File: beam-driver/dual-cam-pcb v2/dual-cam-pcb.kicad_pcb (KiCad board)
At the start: 2 copper layers, 76 x 51 mm, 45 parts, among them J1 Conn_01x08_Pin, J2 Conn_01x08_Pin, J3 Conn_Coaxial, J4 LED connector, J5 LED connector, J6 tilt, J7 pan, J8 Conn_XT_Sink, Q1 Q_NMOS_GDS, U1 Pico, U2 PUCC27624DR, U3 LM317L_SOT-89, U4 LM7805_TO220

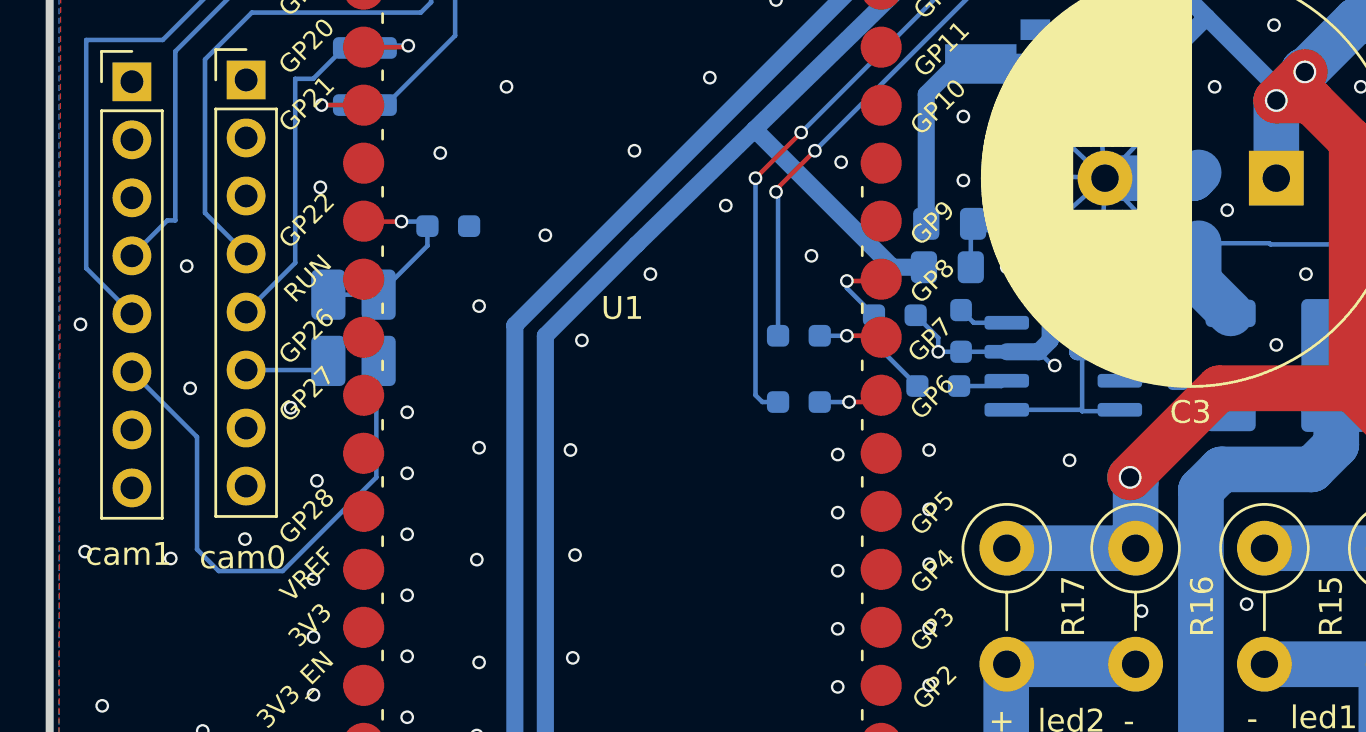
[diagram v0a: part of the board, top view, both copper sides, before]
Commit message: update beam-driver pcb
to include emi filter on ExposureActive camera GPIO.
+ update gerbers
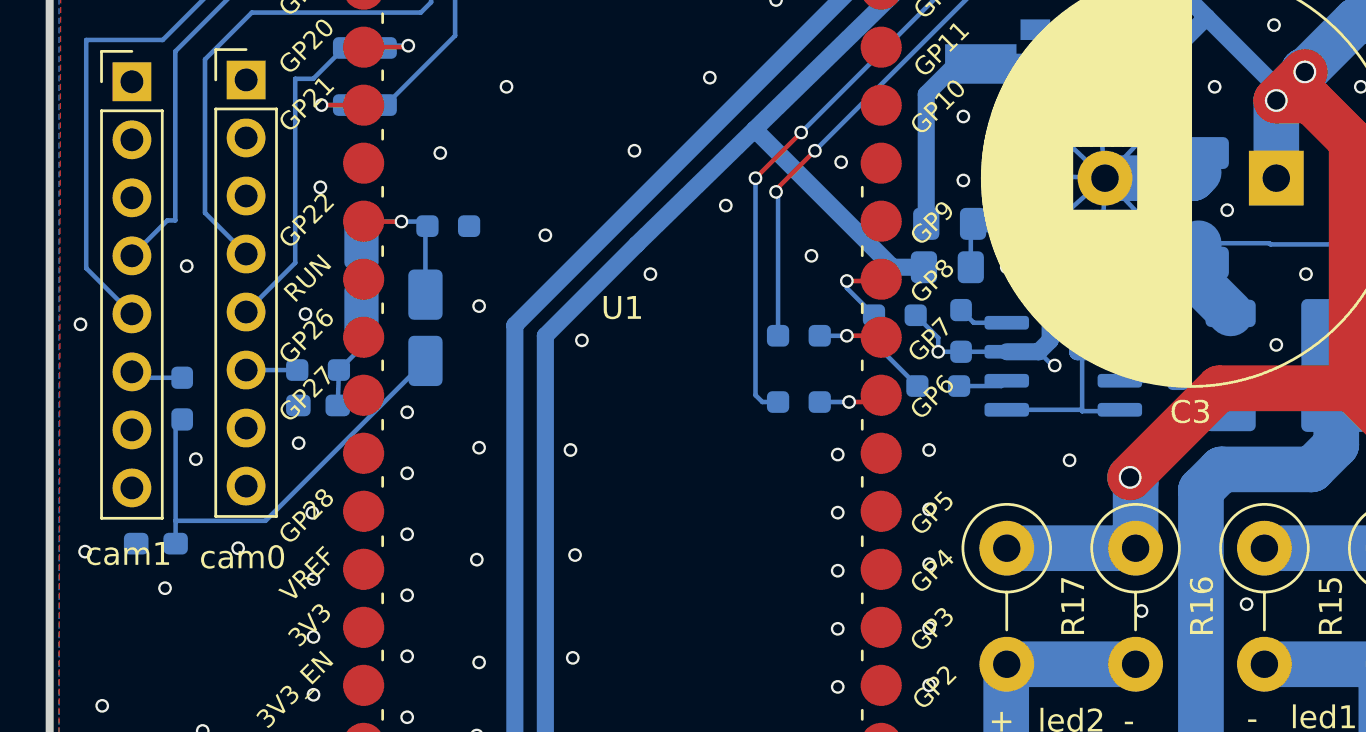
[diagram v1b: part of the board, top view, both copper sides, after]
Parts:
- added C8: 200pF, Capacitor_SMD:C_0603_1608Metric_Pad1.08x0.95mm_HandSolder, B.Cu at (78.5, 92.0)
- added C9: 200pF, Capacitor_SMD:C_0603_1608Metric_Pad1.08x0.95mm_HandSolder, B.Cu at (85.7, 86.0)
- added R20: 1k, Resistor_SMD:R_0603_1608Metric_Pad0.98x0.95mm_HandSolder, B.Cu at (79.7, 85.7)
- added R21: 1k, Resistor_SMD:R_0603_1608Metric_Pad0.98x0.95mm_HandSolder, B.Cu at (85.7, 84.4)
- R1: value 10k -> 20k
- R10: value 10k -> 510
- R12: footprint Resistor_SMD:R_1206_3216Metric_Pad1.30x1.75mm_HandSolder -> Resistor_SMD:R_2010_5025Metric_Pad1.40x2.65mm_HandSolder
- R9: value 10k -> 4k3
- moved D1 2.68 mm to (87.5, 80.3)
- moved D2 2.05 mm to (90.3, 82.5)
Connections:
- J1 pad 6: Net-(D1-A) -> Net-(J1-Pin_6)
- J2 pad 6: Net-(D2-A) -> Net-(J2-Pin_6)
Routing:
- net Net-(D2-A): track 24.0 -> 19.4 mm
- net Net-(J2-Pin_6): track 0.00 -> 2.31 mm
- net Net-(J1-Pin_6): track 0.00 -> 2.24 mm
- net Net-(D1-K): track 9.07 -> 8.16 mm
- net Net-(D1-A): track 3.77 -> 4.61 mm
- net GND: vias 126 -> 127

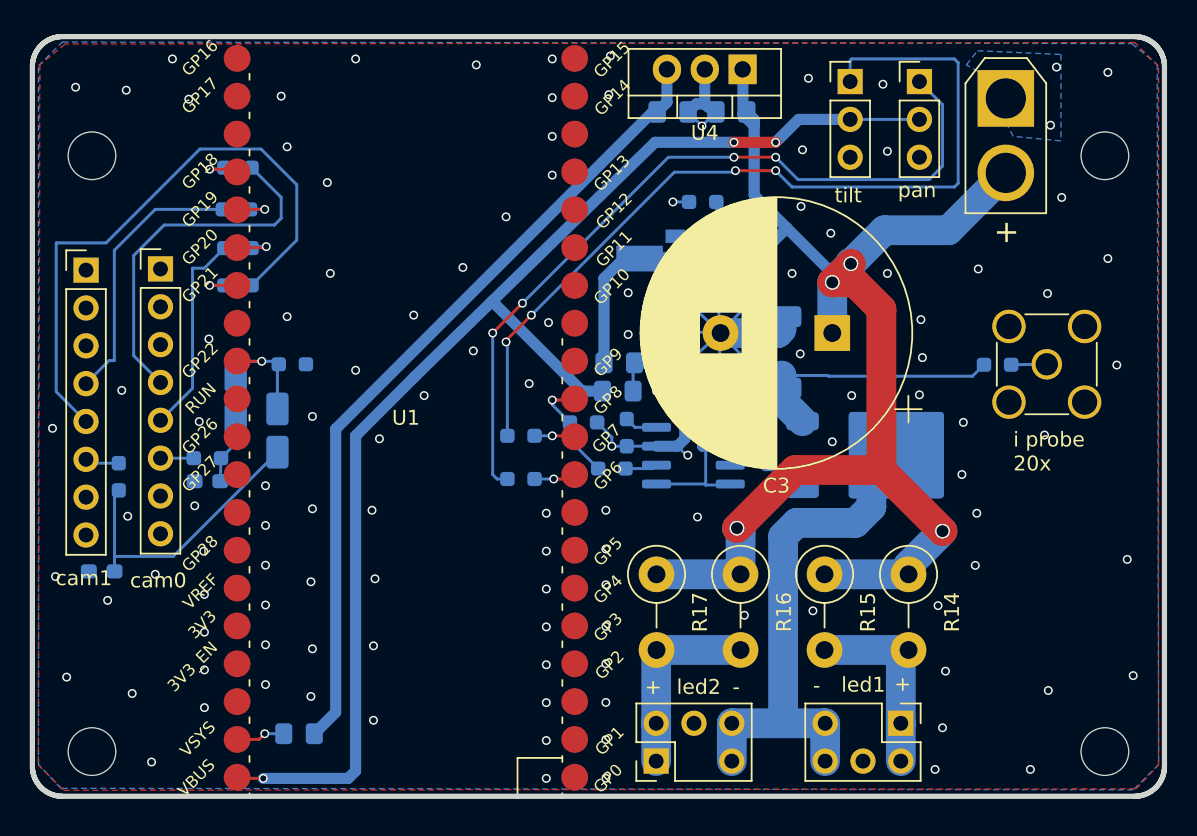
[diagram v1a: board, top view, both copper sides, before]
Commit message: update dual-cam-pcb
* change some footprints
* add miller capacitor (to smooth out led transitions)
* add pcb name
* minor layout changes
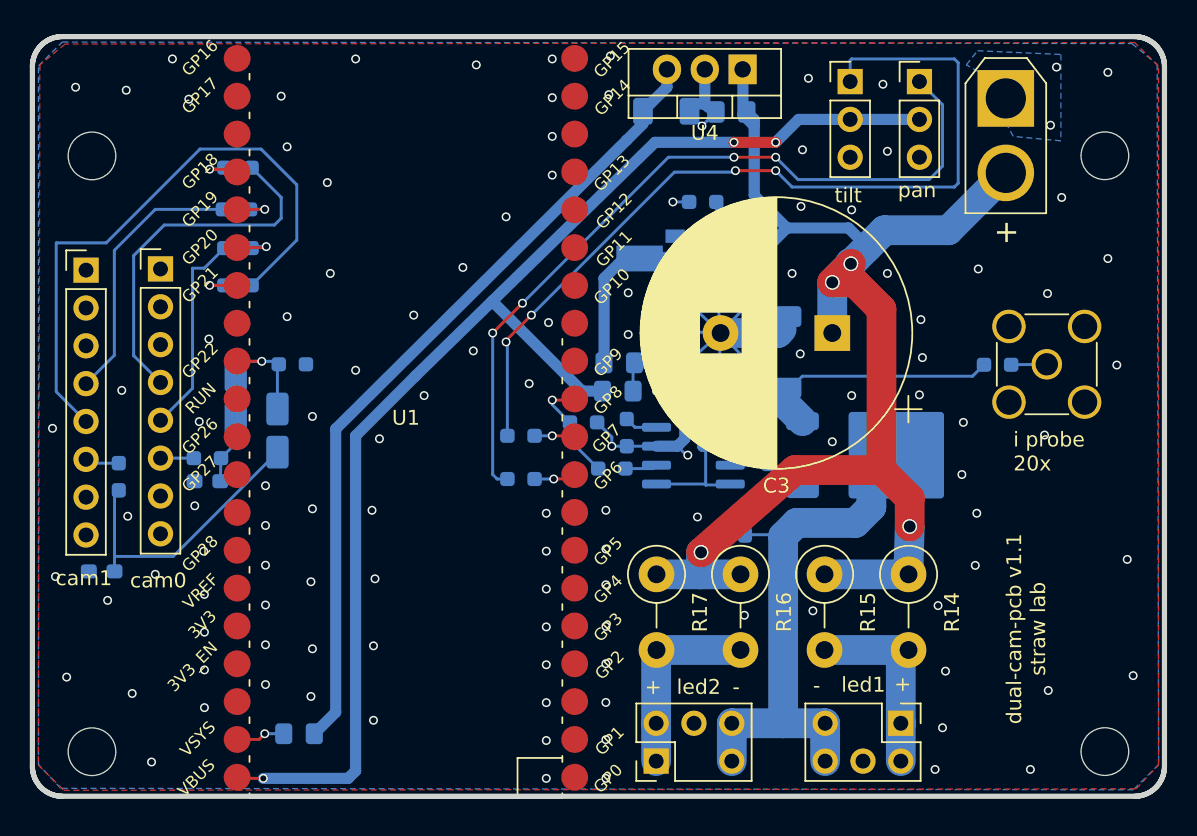
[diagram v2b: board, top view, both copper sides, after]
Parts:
- removed the REF** at (145.9, 64.1)
- removed the REF** at (77.9, 104.1)
- removed the REF** at (145.9, 104.1)
- removed the REF** at (77.9, 64.1)
- added C10: tbd, Capacitor_SMD:C_0603_1608Metric_Pad1.08x0.95mm_HandSolder, B.Cu at (121.7, 88.7)
- added REF**: MountingHole_3.2mm_M3_DIN965, MountingHole:MountingHole_3.2mm_M3_DIN965, F.Cu at (77.9, 64.1)
- added REF**: MountingHole_3.2mm_M3_DIN965, MountingHole:MountingHole_3.2mm_M3_DIN965, F.Cu at (145.9, 64.1)
- added REF**: MountingHole_3.2mm_M3_DIN965, MountingHole:MountingHole_3.2mm_M3_DIN965, F.Cu at (77.9, 104.1)
- added REF**: MountingHole_3.2mm_M3_DIN965, MountingHole:MountingHole_3.2mm_M3_DIN965, F.Cu at (145.9, 104.1)
- C7: footprint Capacitor_SMD:C_0805_2012Metric_Pad1.18x1.45mm_HandSolder -> Capacitor_SMD:C_1206_3216Metric_Pad1.33x1.80mm_HandSolder
- moved C7 0.44 mm to (116.5, 61.1)
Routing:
- net Net-(J4-minus1): track 32.6 -> 35.2 mm
- net Net-(Q1-S): track 17.6 -> 15.2 mm
- net Net-(Q1-G): track 2.35 -> 4.41 mm
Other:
- board text added: "dual-cam-pcb v1.1 straw lab"
